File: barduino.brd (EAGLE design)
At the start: 50.3 x 47.4 mm, 28 parts, among them Q1 16MHz

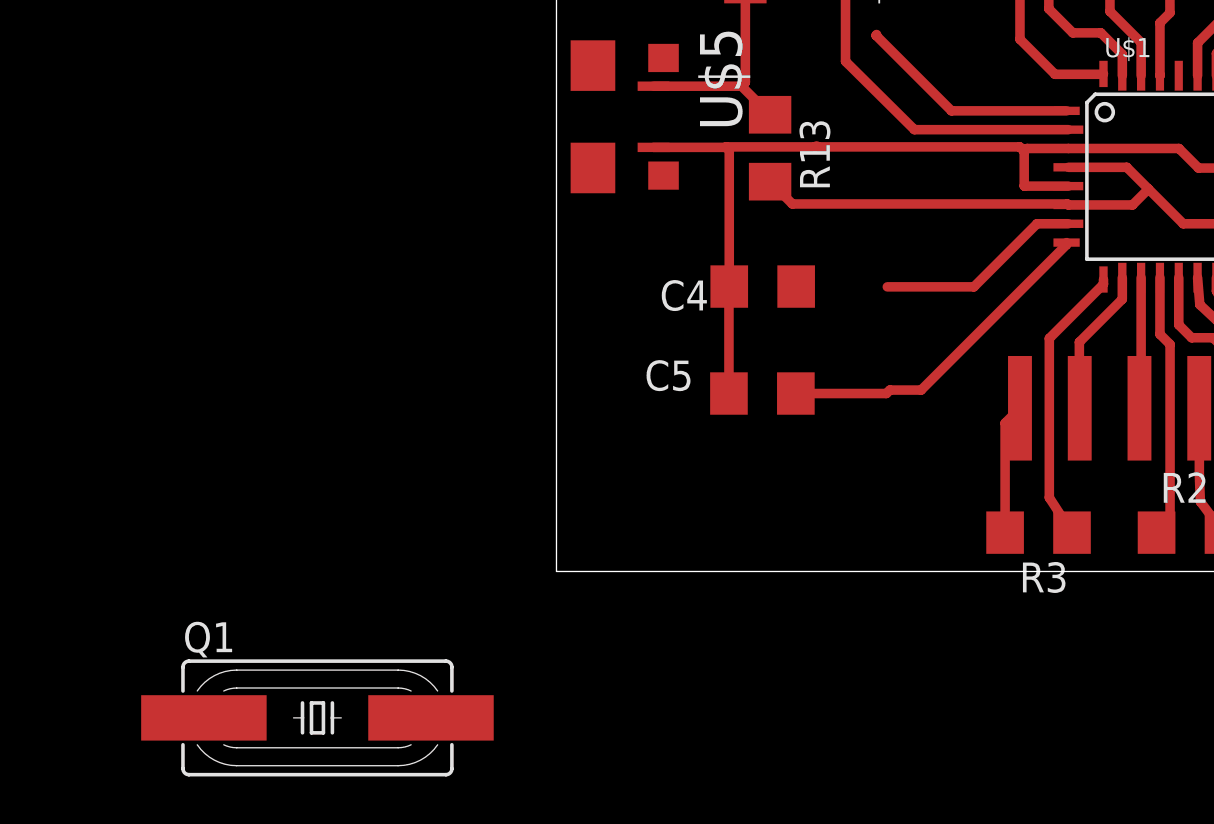
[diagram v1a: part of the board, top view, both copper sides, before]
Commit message: move crystal into place
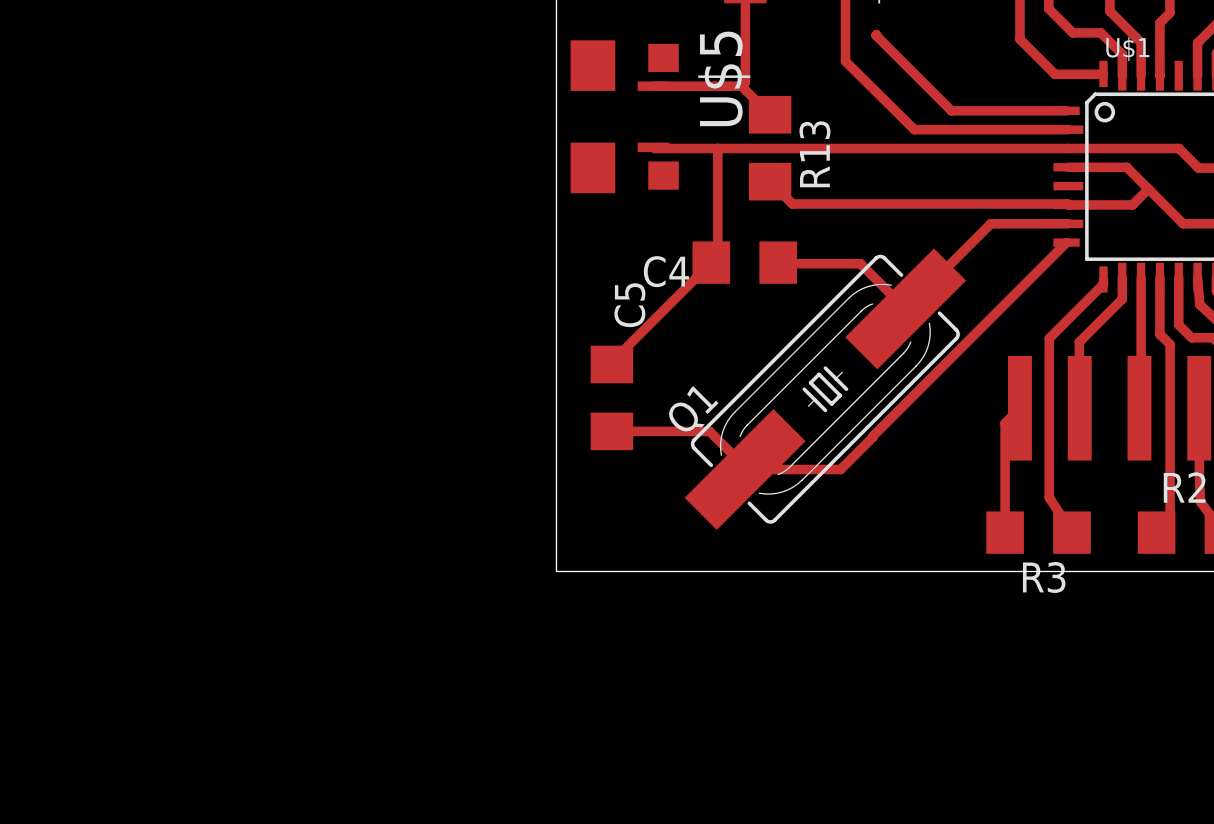
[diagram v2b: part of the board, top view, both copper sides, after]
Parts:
- moved Q1 25.7 mm to (-3.81, 20.1), turned to 45 degrees
- moved C5 6.40 mm to (-12.9, 19.7), turned to 270 degrees
- moved C4 1.27 mm to (-7.24, 25.4)
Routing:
- net PB7: track 14.2 -> 24.1 mm
- net PB6: track 8.84 -> 14.6 mm
- net GND: track 103.4 -> 100.4 mm
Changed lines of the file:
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@@
 </autorouter>
 <elements>
-<element name="C4" library="ng" package="1206" value="18pF" x="-6.4744" y="24.42978125" smashed="yes">
-<attribute name="NAME" x="-8.7604" y="24.68378125" size="1.27" layer="25" rot="R180"/>
-<attribute name="VALUE" x="-7.8714" y="22.01678125" size="1.27" layer="27"/>
-</element>
-<element name="C5" library="ng" package="1206" value="18pF" x="-6.4871" y="19.883175" smashed="yes">
-<attribute name="NAME" x="-9.4081" y="21.280175" size="1.27" layer="25" rot="R180"/>
-<attribute name="VALUE" x="-7.8841" y="17.470175" size="1.27" layer="27"/>
+<element name="C4" library="ng" package="1206" value="18pF" x="-7.2364" y="25.44578125" smashed="yes">
+<attribute name="NAME" x="-9.5224" y="25.69978125" size="1.27" layer="25" rot="R180"/>
+<attribute name="VALUE" x="-8.6334" y="23.03278125" size="1.27" layer="27"/>
+</element>
+<element name="C5" library="ng" package="1206" value="18pF" x="-12.882825" y="19.6951" smashed="yes" rot="R270">
+<attribute name="NAME" x="-11.485825" y="22.6161" size="1.27" layer="25" rot="R90"/>
+<attribute name="VALUE" x="-15.295825" y="21.0921" size="1.27" layer="27" rot="R270"/>
 </element>
 <element name="R9" library="ng" package="1206" value="10K" x="-7.21111875" y="38.68926875" smashed="yes" rot="R270">
@@
 <element name="U$5" library="4-Digit-Clock" package="DX4R005HJ5-PWR" value="MICRO-USB-PWR" x="-15.24" y="31.645859375" rot="R270"/>
 <element name="R13" library="resistor" library_urn="urn:adsk.eagle:library:348" package="R1206" package3d_urn="urn:adsk.eagle:package:26062/1" value="" x="-6.1595" y="30.30981875" rot="R270"/>
-<element name="Q1" library="crystal" library_urn="urn:adsk.eagle:library:204" package="HC49UP" package3d_urn="urn:adsk.eagle:package:12078/1" value="16MHz" x="-25.4" y="6.096">
-<attribute name="MF" value="" x="-25.4" y="6.096" size="1.778" layer="27" display="off"/>
-<attribute name="MPN" value="" x="-25.4" y="6.096" size="1.778" layer="27" display="off"/>
-<attribute name="OC_FARNELL" value="unknown" x="-25.4" y="6.096" size="1.778" layer="27" display="off"/>
-<attribute name="OC_NEWARK" value="unknown" x="-25.4" y="6.096" size="1.778" layer="27" display="off"/>
+<element name="Q1" library="crystal" library_urn="urn:adsk.eagle:library:204" package="HC49UP" package3d_urn="urn:adsk.eagle:package:12078/1" value="16MHz" x="-3.81" y="20.066" rot="R45">
+<attribute name="MF" value="" x="-3.81" y="20.066" size="1.778" layer="27" rot="R45" display="off"/>
+<attribute name="MPN" value="" x="-3.81" y="20.066" size="1.778" layer="27" rot="R45" display="off"/>
+<attribute name="OC_FARNELL" value="unknown" x="-3.81" y="20.066" size="1.778" layer="27" rot="R45" display="off"/>
+<attribute name="OC_NEWARK" value="unknown" x="-3.81" y="20.066" size="1.778" layer="27" rot="R45" display="off"/>
 </element>
 </elements>
@@
 <wire x1="29.94151875" y1="36.210240625" x2="29.94151875" y2="34.7265" width="0.4064" layer="1"/>
 <wire x1="29.94151875" y1="34.7265" x2="29.953934375" y2="34.714084375" width="0.4064" layer="1"/>
-<wire x1="-7.9091" y1="24.41708125" x2="-7.9091" y2="19.883175" width="0.4064" layer="1"/>
-<wire x1="-7.9091" y1="24.41708125" x2="-7.8964" y2="24.42978125" width="0.4064" layer="1"/>
 <contactref element="U$1" pad="21"/>
 <contactref element="U$1" pad="3"/>
@@
 <wire x1="19.353825" y1="29.4983" x2="19.705265625" y2="29.849740625" width="0.4064" layer="1"/>
 <wire x1="19.705265625" y1="29.849740625" x2="19.64430625" y2="30.04814375" width="0.4064" layer="1"/>
-<wire x1="4.64058125" y1="30.177740625" x2="4.64058125" y2="28.71110625" width="0.4064" layer="1"/>
-<wire x1="6.5177" y1="28.6983" x2="4.6533875" y2="28.6983" width="0.4064" layer="1"/>
-<wire x1="4.6533875" y1="28.6983" x2="4.64058125" y2="28.71110625" width="0.4064" layer="1"/>
-<wire x1="-8.016240625" y1="30.3659" x2="-4.254496875" y2="30.3659" width="0.4064" layer="1"/>
-<wire x1="4.452421875" y1="30.3659" x2="4.64058125" y2="30.177740625" width="0.4064" layer="1"/>
-<wire x1="-7.8964" y1="24.42978125" x2="-7.8964" y2="30.246059375" width="0.4064" layer="1"/>
-<wire x1="-7.8964" y1="30.246059375" x2="-8.016240625" y2="30.3659" width="0.4064" layer="1"/>
 <contactref element="U$4" pad="P$2"/>
-<wire x1="6.5177" y1="30.2983" x2="4.761140625" y2="30.2983" width="0.4064" layer="1"/>
-<wire x1="4.761140625" y1="30.2983" x2="4.64058125" y2="30.177740625" width="0.4064" layer="1"/>
 <wire x1="19.65190625" y1="50.906009375" x2="19.558" y2="51.054" width="0.4064" layer="1"/>
-<wire x1="-4.183378125" y1="30.406540625" x2="-37.64471875" y2="51.3562625" width="0" layer="19" extent="1-16"/>
-<wire x1="-4.183378125" y1="30.406540625" x2="-4.254496875" y2="30.3659" width="0.4064" layer="1"/>
-<wire x1="-4.254496875" y1="30.3659" x2="4.452421875" y2="30.3659" width="0.4064" layer="1"/>
 <wire x1="19.705265625" y1="29.849740625" x2="22.425321875" y2="29.849740625" width="0.4064" layer="1"/>
 <wire x1="22.425321875" y1="29.849740625" x2="24.60498125" y2="32.0294" width="0.4064" layer="1"/>
@@
 <wire x1="24.64054375" y1="40.17771875" x2="24.64054375" y2="46.24249375" width="0.4064" layer="1"/>
 <wire x1="24.64054375" y1="46.24249375" x2="19.65190625" y2="50.906009375" width="0.4064" layer="1"/>
-<wire x1="-8.0924375" y1="30.3430375" x2="-8.016240625" y2="30.3659" width="0.4064" layer="1"/>
 <contactref element="R11" pad="2"/>
-<wire x1="-37.64471875" y1="51.3562625" x2="-4.23671875" y2="42.341403125" width="0" layer="19" extent="1-16"/>
 <wire x1="-4.23671875" y1="42.341403125" x2="-5.76111875" y2="43.865803125" width="0.4064" layer="1"/>
 <contactref element="U$5" pad="GND"/>
-<wire x1="-11.115" y1="30.345859375" x2="-8.03628125" y2="30.345859375" width="0.4064" layer="1"/>
-<wire x1="-8.03628125" y1="30.345859375" x2="-8.016240625" y2="30.3659" width="0.4064" layer="1"/>
+<wire x1="6.5177" y1="30.2983" x2="-8.382" y2="30.2983" width="0.4064" layer="1"/>
+<wire x1="-8.382" y1="30.2983" x2="-11.067440625" y2="30.2983" width="0.4064" layer="1"/>
+<wire x1="-11.067440625" y1="30.2983" x2="-11.115" y2="30.345859375" width="0.4064" layer="1"/>
+<wire x1="-12.882825" y1="21.47535625" x2="-12.882825" y2="21.1171" width="0.4064" layer="1"/>
+<wire x1="-8.382" y1="30.2983" x2="-8.382" y2="25.72218125" width="0.4064" layer="1"/>
+<wire x1="-8.382" y1="25.72218125" x2="-8.6584" y2="25.44578125" width="0.4064" layer="1"/>
+<wire x1="-8.6584" y1="25.44578125" x2="-12.628825" y2="21.47535625" width="0.4064" layer="1"/>
+<wire x1="-12.628825" y1="21.47535625" x2="-12.882825" y2="21.47535625" width="0.4064" layer="1"/>
+<wire x1="-8.382" y1="30.2983" x2="-4.23671875" y2="42.341403125" width="0" layer="19" extent="1-1"/>
+<wire x1="6.5177" y1="28.6983" x2="6.5177" y2="30.2983" width="0" layer="19" extent="1-1"/>
+<wire x1="-37.64471875" y1="51.3562625" x2="-5.76111875" y2="43.865803125" width="0" layer="19" extent="1-1"/>
 </signal>
 <signal name="PB7">
 <contactref element="C5" pad="2"/>
 <contactref element="U$1" pad="8"/>
-<wire x1="6.4415" y1="26.2983" x2="6.4415" y2="26.210321875" width="0.4064" layer="1"/>
-<wire x1="6.4415" y1="26.210321875" x2="0.26161875" y2="20.030440625" width="0.4064" layer="1"/>
-<wire x1="-1.069340625" y1="20.030440625" x2="0.26161875" y2="20.030440625" width="0.4064" layer="1"/>
-<wire x1="-5.0651" y1="19.883175" x2="-1.21660625" y2="19.883175" width="0.4064" layer="1"/>
-<wire x1="-1.21660625" y1="19.883175" x2="-1.069340625" y2="20.030440625" width="0.4064" layer="1"/>
 <contactref element="Q1" pad="1"/>
-<wire x1="-5.0651" y1="19.883175" x2="-30.226" y2="6.096" width="0" layer="19" extent="1-1"/>
+<wire x1="6.4415" y1="26.2983" x2="-1.778" y2="18.0788" width="0.4064" layer="1"/>
+<wire x1="-1.778" y1="18.0788" x2="-1.778" y2="18.034" width="0.4064" layer="1"/>
+<wire x1="-1.778" y1="18.034" x2="-3.1585" y2="16.6535" width="0.4064" layer="1"/>
+<wire x1="-3.1585" y1="16.6535" x2="-7.112" y2="16.6535" width="0.4064" layer="1"/>
+<wire x1="-7.112" y1="16.6535" x2="-7.222496875" y2="16.6535" width="0.4064" layer="1"/>
+<wire x1="-12.882825" y1="18.2731" x2="-8.7316" y2="18.2731" width="0.4064" layer="1"/>
+<wire x1="-8.7316" y1="18.2731" x2="-7.112" y2="16.6535" width="0.4064" layer="1"/>
 </signal>
 <signal name="RESET">
@@
 <signal name="PB6">
 <contactref element="C4" pad="2"/>
-<wire x1="5.18318125" y1="27.0983" x2="2.5019" y2="24.41701875" width="0.4064" layer="1"/>
-<wire x1="2.5019" y1="24.41701875" x2="-1.1785625" y2="24.41701875" width="0.4064" layer="1"/>
-<wire x1="-5.027" y1="24.40438125" x2="-5.0524" y2="24.42978125" width="0.4064" layer="1"/>
 <contactref element="U$1" pad="7"/>
-<wire x1="6.5177" y1="27.0983" x2="5.18318125" y2="27.0983" width="0.4064" layer="1"/>
 <contactref element="Q1" pad="2"/>
-<wire x1="-5.027" y1="24.40438125" x2="-1.1785625" y2="24.41701875" width="0" layer="19" extent="1-1"/>
-<wire x1="-20.574" y1="6.096" x2="-5.0524" y2="24.42978125" width="0" layer="19" extent="1-1"/>
+<wire x1="6.5177" y1="27.0983" x2="3.222303125" y2="27.0983" width="0.4064" layer="1"/>
+<wire x1="3.222303125" y1="27.0983" x2="-0.3975" y2="23.478496875" width="0.4064" layer="1"/>
+<wire x1="-5.8144" y1="25.44578125" x2="-5.76861875" y2="25.4" width="0.4064" layer="1"/>
+<wire x1="-2.319003125" y1="25.4" x2="-0.3975" y2="23.478496875" width="0.4064" layer="1"/>
+<wire x1="-5.76861875" y1="25.4" x2="-2.319003125" y2="25.4" width="0.4064" layer="1"/>
 </signal>
 <signal name="D0">

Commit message: rip up some wires
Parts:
- moved R11 30.0 mm to (-36.9, 39.8)
- moved U$4 25.2 mm to (-6.78, 42.0), turned to 160 degrees
- moved R9 23.7 mm to (-30.1, 32.3)
- moved LED1 3.56 mm to (27.9, 54.4)
- moved LED2 3.56 mm to (-7.06, 54.4)
- moved R10 2.55 mm to (-3.26, 50.8)
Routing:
- net RESET: track 102.3 -> 58.6 mm
- net D4: track 23.5 -> 10.7 mm
- net N$3: track 37.3 -> 26.7 mm
- net D3: track 9.47 -> 0.00 mm
- net N$2: track 7.02 -> 0.00 mm
- net VCC: track 83.6 -> 78.7 mm
- net N$1: track 7.99 -> 10.9 mm
- net GND: track 100.4 -> 98.3 mm

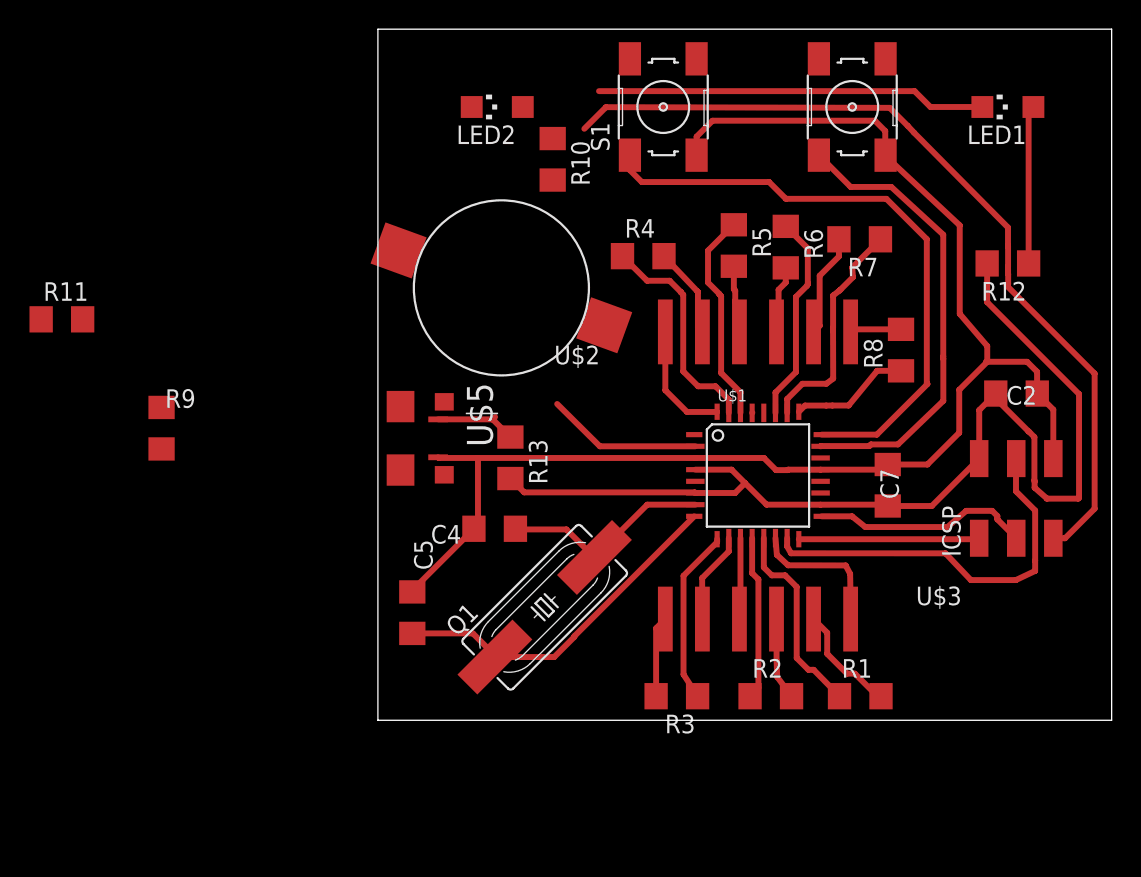
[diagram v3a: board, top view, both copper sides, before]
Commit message: go back to original board size
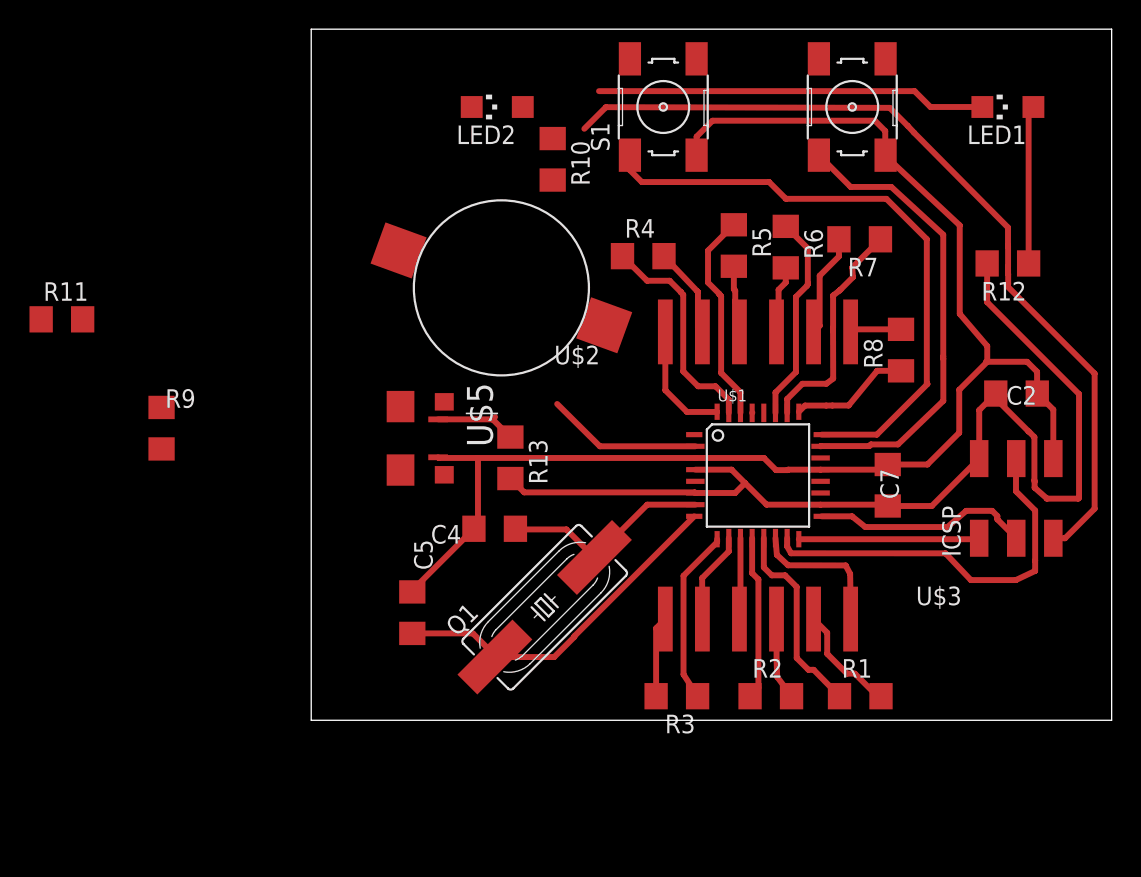
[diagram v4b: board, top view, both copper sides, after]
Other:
- board size 50.3 x 47.4 mm -> 54.9 x 47.4 mm
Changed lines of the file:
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@@
 <board>
 <plain>
-<wire x1="-15.24" y1="12.319" x2="35.052" y2="12.319" width="0" layer="20"/>
+<wire x1="-19.812" y1="12.319" x2="35.052" y2="12.319" width="0" layer="20"/>
 <wire x1="35.052" y1="12.319" x2="35.052" y2="59.69" width="0" layer="20"/>
-<wire x1="35.052" y1="59.69" x2="-15.24" y2="59.69" width="0" layer="20"/>
-<wire x1="-15.24" y1="59.69" x2="-15.24" y2="12.319" width="0" layer="20"/>
+<wire x1="35.052" y1="59.69" x2="-19.812" y2="59.69" width="0" layer="20"/>
+<wire x1="-19.812" y1="59.69" x2="-19.812" y2="12.319" width="0" layer="20"/>
 </plain>
 <attributes>

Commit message: connected most signals
still some air wires left
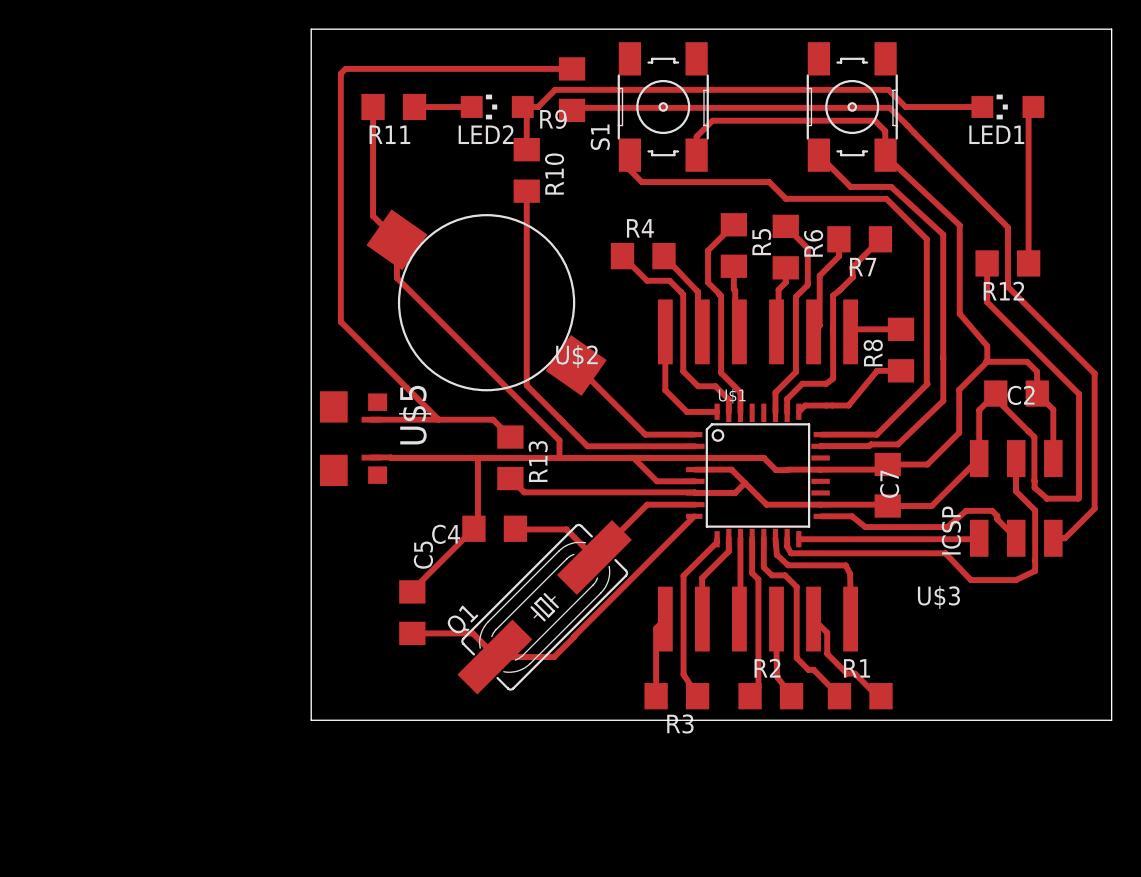
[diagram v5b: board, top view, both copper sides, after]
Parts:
- moved R9 36.5 mm to (-1.93, 55.5), turned to 90 degrees
- moved R11 27.0 mm to (-14.2, 54.4), turned to 180 degrees
- moved U$5 4.57 mm to (-19.8, 31.6)
- moved R10 1.93 mm to (-5.04, 50.0)
- moved U$4 1.44 mm to (-7.79, 40.9), turned to 145 degrees
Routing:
- net VCC: track 78.7 -> 125.5 mm
- net GND: track 98.3 -> 137.3 mm
- net D4: track 10.7 -> 26.6 mm
- net D3: track 0.00 -> 10.1 mm
- net N$3: track 26.7 -> 35.5 mm
- net N$2: track 0.00 -> 3.92 mm
